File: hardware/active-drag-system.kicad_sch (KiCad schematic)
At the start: 15 parts, among them J1 Conn_01x02_Pin, J2 Conn_01x02_Socket, J3 10118193-0001LF, J4 Conn_01x05_Pin, J5 Conn_01x02_Pin, J6 Conn_01x02_Pin, J7 Conn_01x03_Pin, J8 Conn_01x03_Pin

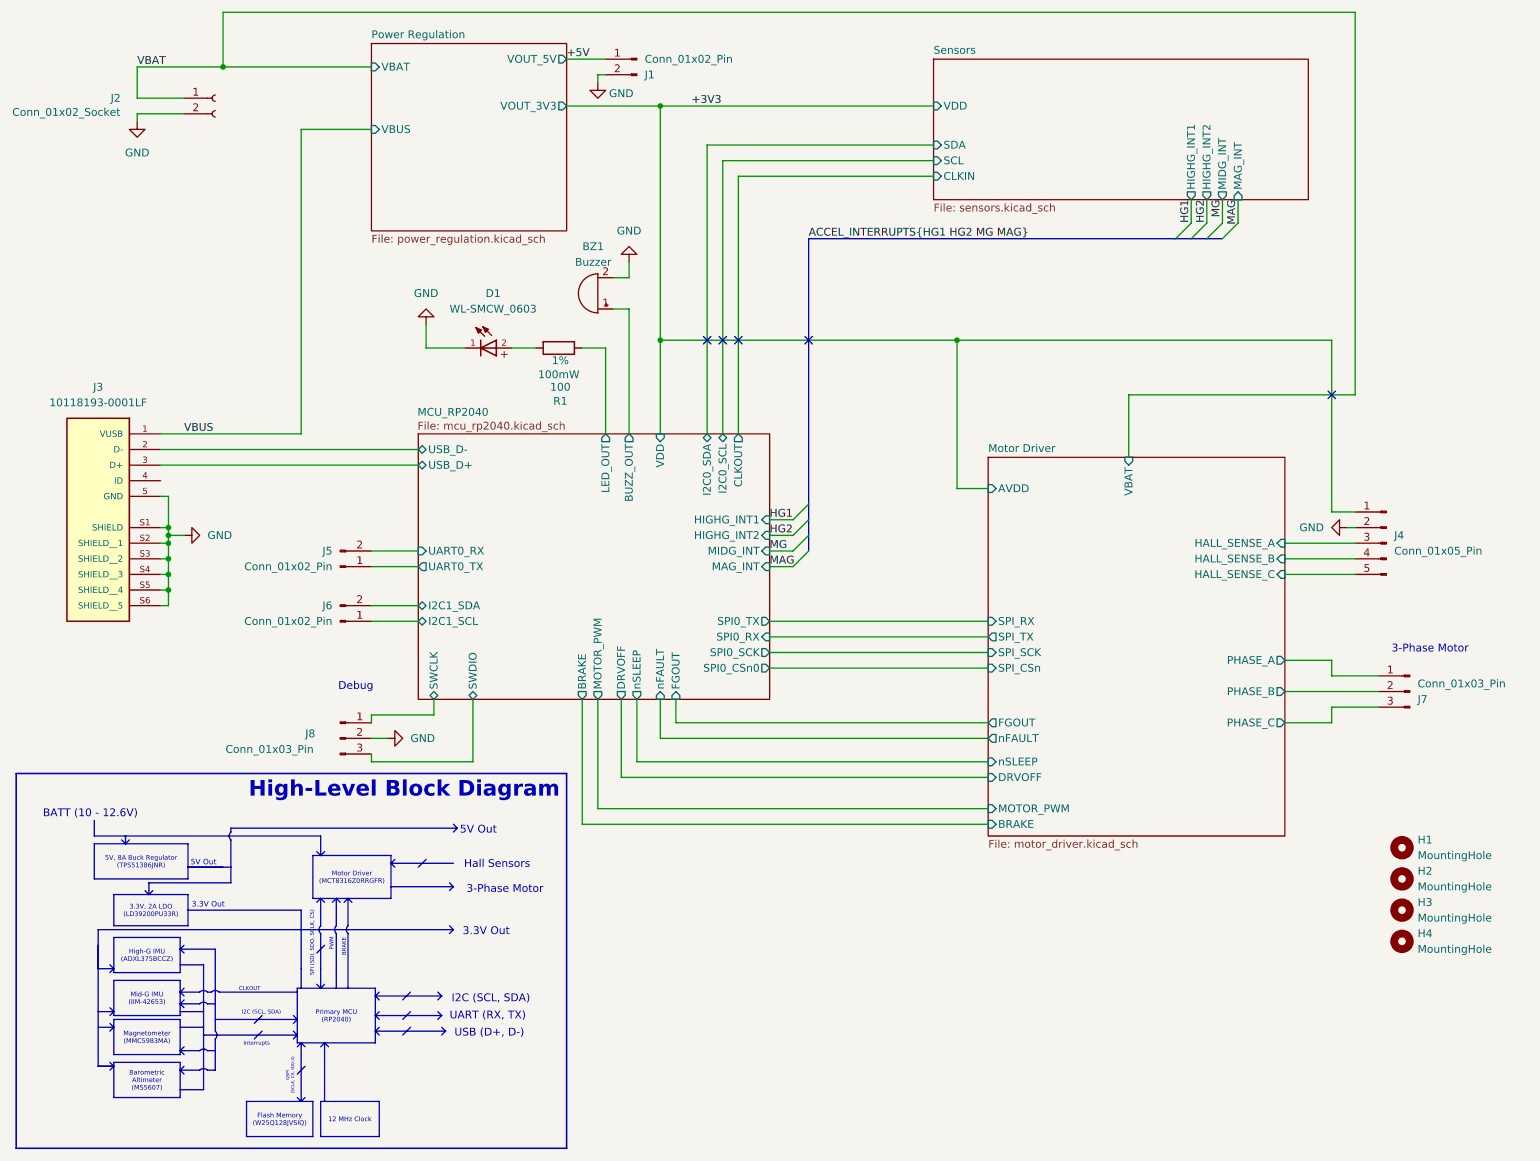
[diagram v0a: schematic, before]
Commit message: Rev 2 of Custom PCB but without Motor Driver (Replaced with Optocoupler Circuit for Standard Servo) (#15)
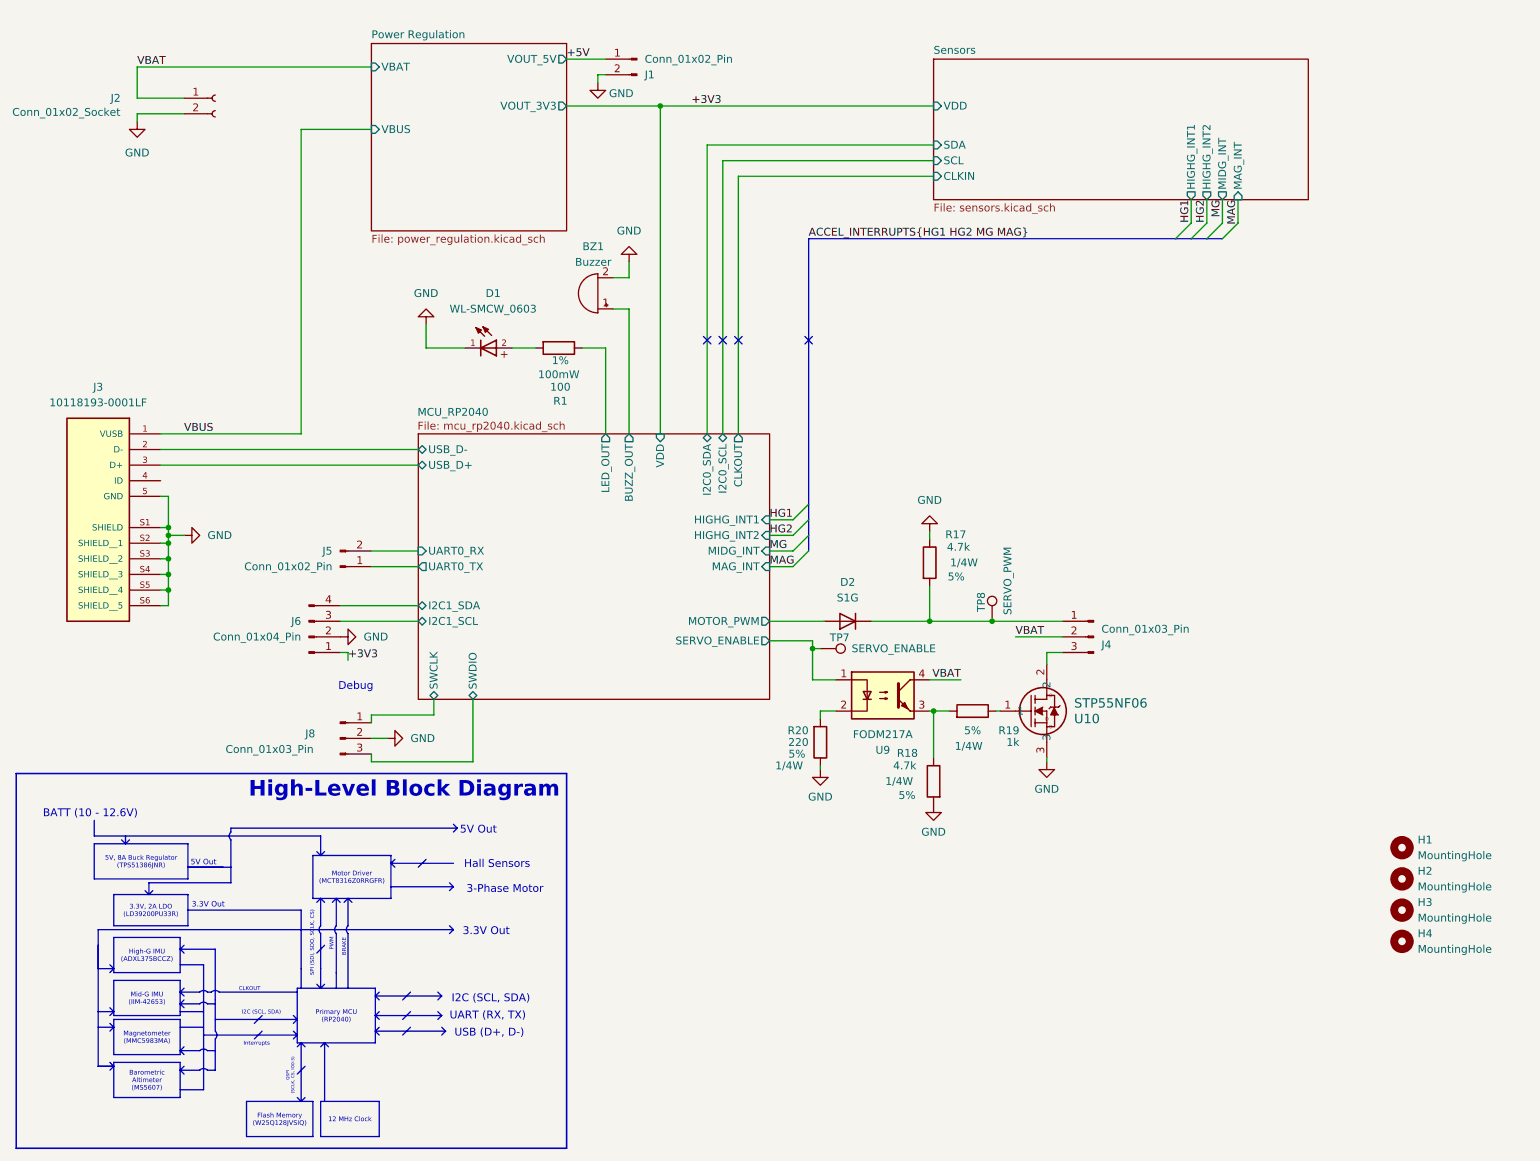
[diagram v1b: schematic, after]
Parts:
- removed J4: Conn_01x05_Pin, Connector_PinHeader_2.54mm:PinHeader_1x05_P2.54mm_Vertical, symbol Connector:Conn_01x05_Pin
- removed J6: Conn_01x02_Pin, Connector_PinHeader_2.54mm:PinHeader_1x02_P2.54mm_Vertical, symbol Connector:Conn_01x02_Pin
- removed J7: Conn_01x03_Pin, active-drag-system:SolderWire-2sqmm_1x03_P7.8mm_D2mm_OD3.9mm, symbol Connector:Conn_01x03_Pin
- added D2: S1G, Diode_SMD:D_SMA, symbol Device:D
- added J4: Conn_01x03_Pin, Connector_PinHeader_2.54mm:PinHeader_1x03_P2.54mm_Vertical, symbol Connector:Conn_01x03_Pin
- added J6: Conn_01x04_Pin, Connector_PinHeader_2.54mm:PinHeader_1x04_P2.54mm_Vertical, symbol Connector:Conn_01x04_Pin
- added R17, R18: 4.7k, Resistor_SMD:R_1206_3216Metric, symbol Device:R
- added R19: 1k, Resistor_SMD:R_1206_3216Metric, symbol Device:R
- added R20: 220, Resistor_SMD:R_1206_3216Metric, symbol Device:R
- added TP7: SERVO_ENABLE, TestPoint:TestPoint_Pad_1.0x1.0mm, symbol Connector:TestPoint
- added TP8: SERVO_PWM, TestPoint:TestPoint_Pad_1.0x1.0mm, symbol Connector:TestPoint
- added U10: STP55NF06, active-drag-system:STP55NF06, symbol active-drag-system:STP55NF06
- added U9: FODM217A, Package_SO:SOP-4_4.4x2.6mm_P1.27mm, symbol Isolator:FODM217A
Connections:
- net +3V3: now also J6.1 (Pin_1)
- net GND: now also J6.2 (Pin_2), R17.1, R18.2, R20.1, U10.3
- net MCU_RP2040/I2C1_SCL: now also J6.3 (Pin_3)
- net MCU_RP2040/I2C1_SDA: now also J6.4 (Pin_4)
- net MCU_RP2040/MOTOR_PWM: now also D2.2 (A)
- net VBAT: now also J4.2 (Pin_2), U9.4
- new net: D2.1 (K), J4.1 (Pin_1), R17.2, TP8.1
- new net: J4.3 (Pin_3), U10.2
- new net: R19.1, U10.1
- new net: R18.1, R19.2, U9.3
- new net: R20.2, U9.2
- new net MCU_RP2040/SERVO_ENABLE: TP7.1, U9.1
- no-connect marks 5 -> 4
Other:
- removed sheet Motor Driver
- sheet MCU_RP2040 ports: added SERVO_ENABLE; removed BRAKE, DRVOFF, FGOUT, SPI0_CSn0, SPI0_RX, SPI0_SCK, SPI0_TX, nFAULT, nSLEEP
